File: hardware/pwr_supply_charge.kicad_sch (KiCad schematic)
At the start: 26 parts, among them J1 USB_C_Receptacle_USB2.0_14P, J2 Battery Input, J3 Power Switch, Q1 AO4435, Q2 AO4406A, Q3 AO4406A, Q4 AO4468, U1 CN3302, U2 HY2120

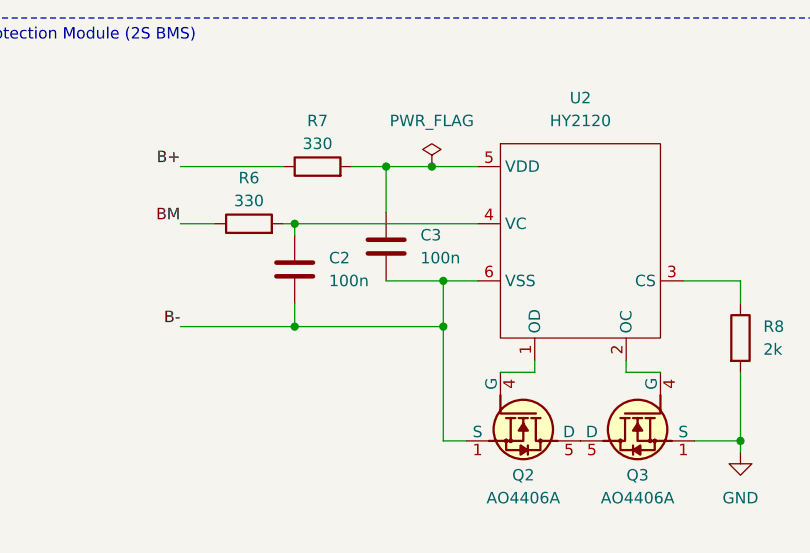
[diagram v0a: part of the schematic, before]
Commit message: Adding power LED status
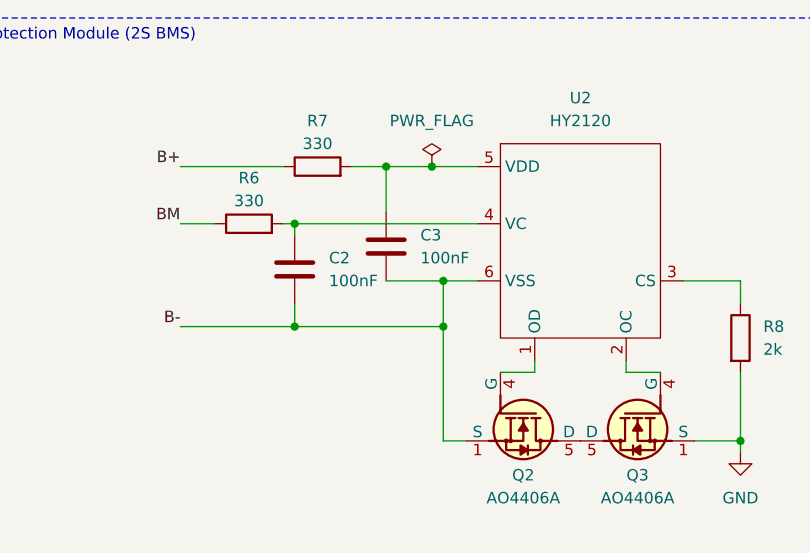
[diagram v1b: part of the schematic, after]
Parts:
- C2, C3: value 100n -> 100nF
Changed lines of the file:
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@@
 			)
 		)
-		(property "Value" "100n"
+		(property "Value" "100nF"
 			(at 180.34 41.9099 0)
 			(effects
@@
 			)
 		)
-		(property "Value" "100n"
+		(property "Value" "100nF"
 			(at 170.18 44.4499 0)
 			(effects

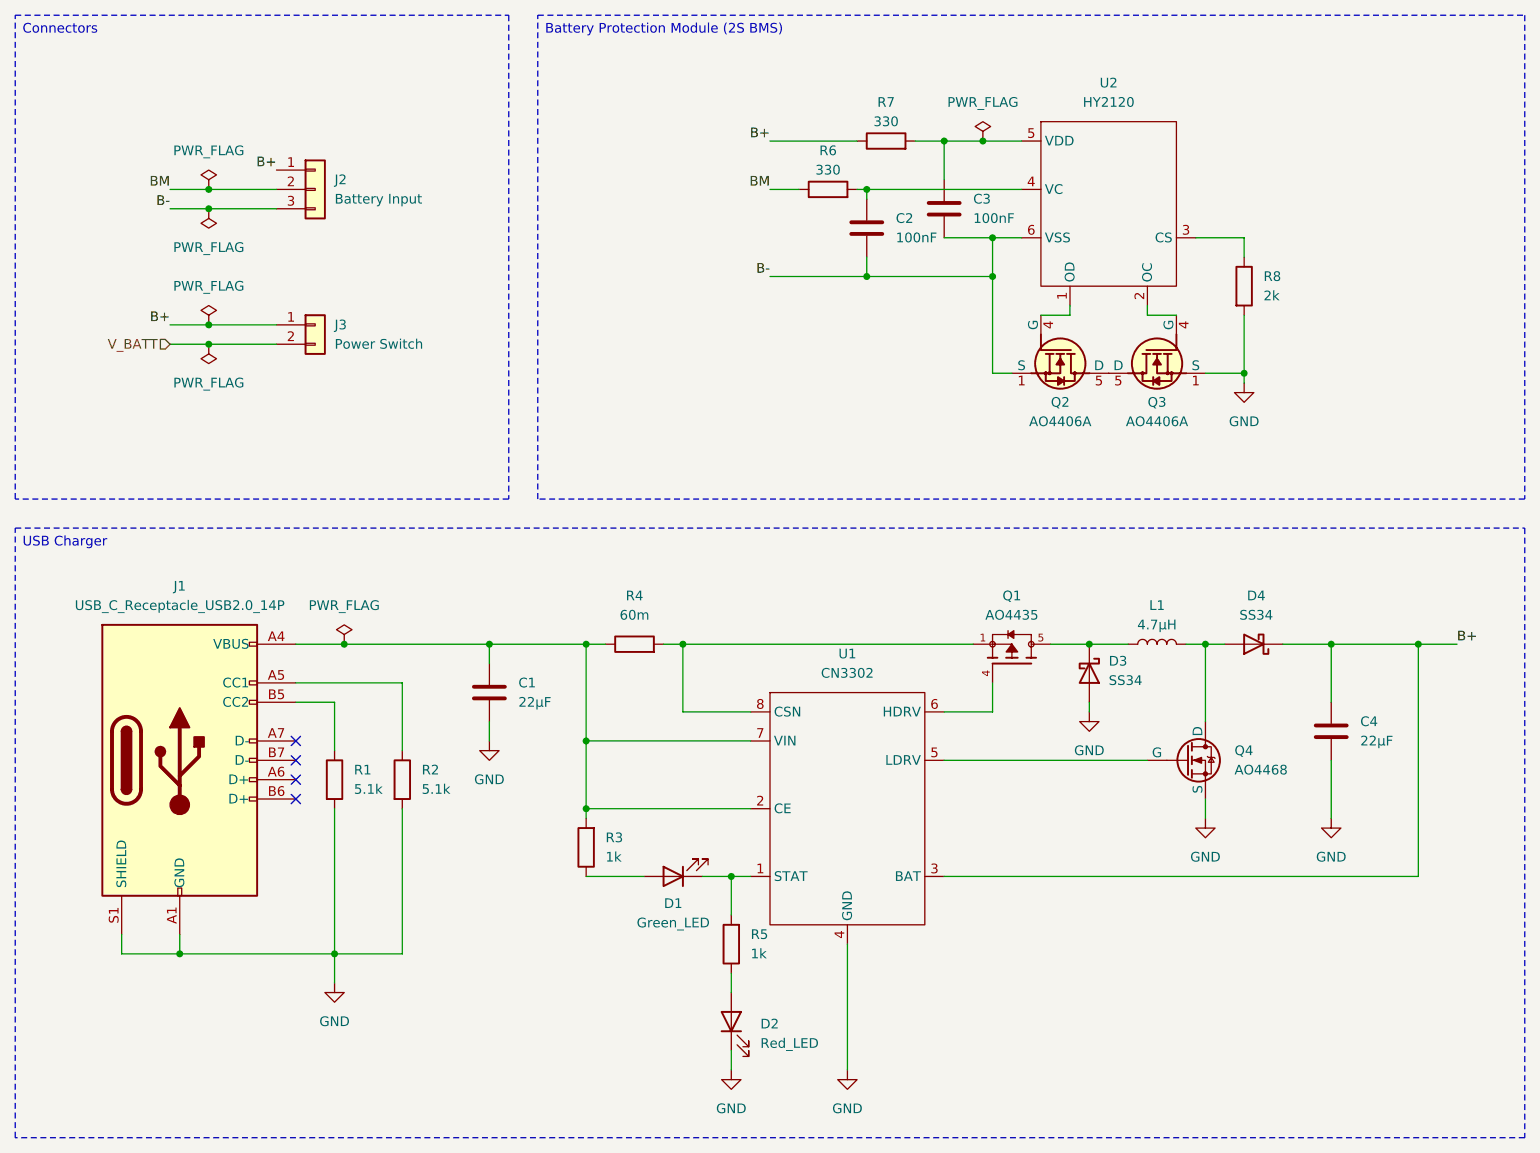
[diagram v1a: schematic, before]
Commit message: Adding footprint & symbol folders
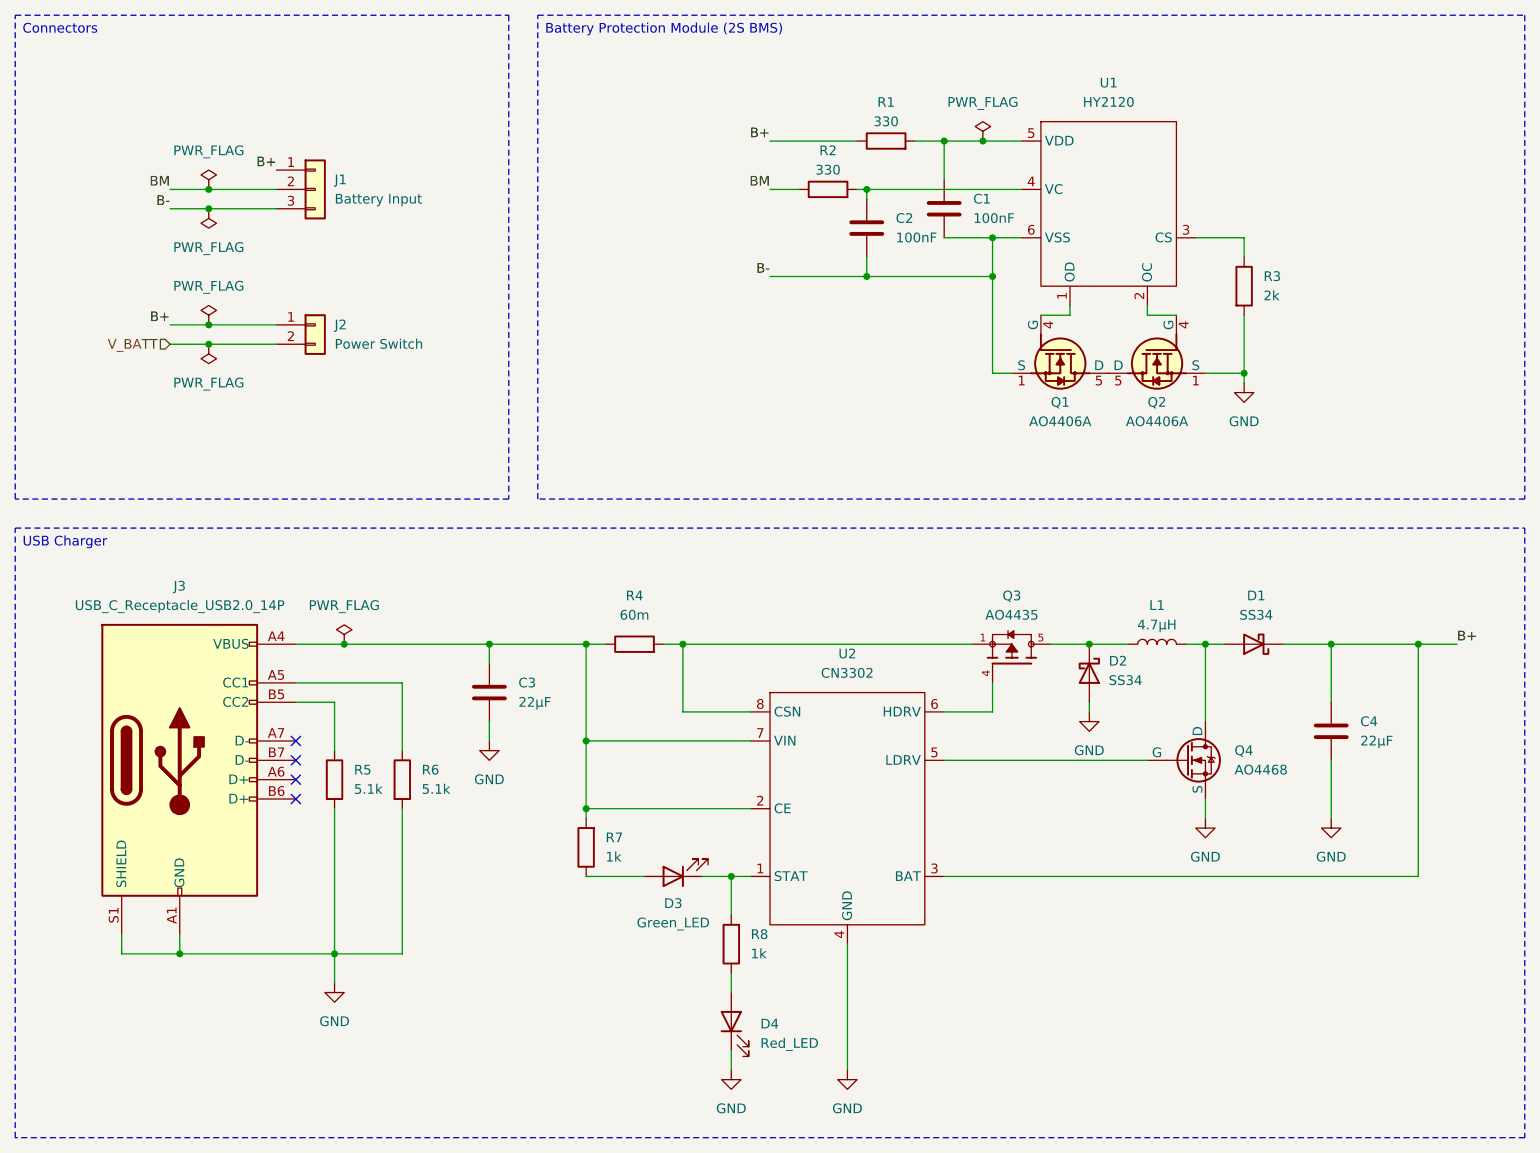
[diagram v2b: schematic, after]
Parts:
- removed Q1: AO4435, AO4435:SOIC127P600X175-8N, symbol AO4435:AO4435
- removed Q2, Q3: AO4406A, AO4406A:SOIC-8_3.9x4.9x1.75mm_P1.27mm, symbol AO4406A:AO4406A
- removed U1: CN3302, symbol _CN3302:CN3302
- removed U2: HY2120, symbol _HY2120:HY2120
- added Q1, Q2: AO4406A, Chromapi_FP:ao4406a_SOIC-8_3.9x4.9x1.75mm_P1.27mm, symbol ao4406a:AO4406A
- added Q3: AO4435, Chromapi_FP:ao4435_SOIC127P600X175-8N, symbol ao4435:AO4435
- added U1: HY2120, symbol hy2120:HY2120
- added U2: CN3302, symbol cn3302:CN3302
- renumbered C3 to C1, C1 to C3, D4 to D1, D3 to D2, D1 to D3, D2 to D4, J2 to J1, J3 to J2, J1 to J3, R7 to R1, R6 to R2, R8 to R3, R1 to R5, R2 to R6, R3 to R7, R5 to R8
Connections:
- net B+: now also U2.3 (BAT)
- net B-: now also Q1.1 (S), Q1.2 (S), Q1.3 (S), U1.6 (VSS)
- net GND: now also Q2.1 (S), Q2.2 (S), Q2.3 (S), U2.4 (GND)
- net at C1.1, R1.2: now also U1.5 (VDD)
- net at D3.1 (K), R8.2: now also U2.1 (STAT)
- net at R4.2: now also Q3.1, Q3.2, Q3.3, U2.8 (CSN)
- net at D2.1 (K), L1.1: now also Q3.5, Q3.6, Q3.7, Q3.8
- net at C3.1, J3.A4 (VBUS), J3.A9 (VBUS)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: now also U2.2 (CE), U2.7 (VIN)
- net at C2.1, R2.2: now also U1.4 (VC)
- net at R3.1: now also U1.3 (CS)
- net at Q4.2 (G): now also U2.5 (LDRV)
- new net: Q1.4 (G), U1.1 (OD)
- new net: Q2.4 (G), U1.2 (OC)
- new net: Q1.5 (D), Q1.6 (D), Q1.7 (D), Q1.8 (D), Q2.5 (D), Q2.6 (D), Q2.7 (D), Q2.8 (D)
- new net: Q3.4, U2.6 (HDRV)

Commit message: Adding cooling fan
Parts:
- D3, D4: footprint (none) -> LED_SMD:LED_0603_1608Metric
- J3: footprint (none) -> Connector_USB:USB_C_Receptacle_HRO_TYPE-C-31-M-12
- Q4: footprint (none) -> Chromapi_FP:ao4435_SOIC127P600X175-8N
- R5, R6, R7, R8: footprint (none) -> Resistor_SMD:R_0603_1608Metric
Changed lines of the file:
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@@
 			)
 		)
-		(property "Footprint" ""
+		(property "Footprint" "LED_SMD:LED_0603_1608Metric"
 			(at 140.97 128.27 0)
 			(effects
@@
 			)
 		)
-		(property "Footprint" ""
+		(property "Footprint" "Resistor_SMD:R_0603_1608Metric"
 			(at 150.368 137.16 90)
 			(effects
@@
 			)
 		)
-		(property "Footprint" ""
+		(property "Footprint" "Resistor_SMD:R_0603_1608Metric"
 			(at 131.318 124.46 90)
 			(effects
@@
 			)
 		)
-		(property "Footprint" ""
+		(property "Footprint" "Resistor_SMD:R_0603_1608Metric"
 			(at 94.742 115.57 90)
 			(effects
@@
 			)
 		)
-		(property "Footprint" ""
+		(property "Footprint" "Resistor_SMD:R_0603_1608Metric"
 			(at 103.632 115.57 90)
 			(effects
@@
 			)
 		)
-		(property "Footprint" ""
+		(property "Footprint" "Chromapi_FP:ao4435_SOIC127P600X175-8N"
 			(at 213.36 110.49 0)
 			(effects
@@
 			)
 		)
-		(property "Footprint" ""
+		(property "Footprint" "Connector_USB:USB_C_Receptacle_HRO_TYPE-C-31-M-12"
 			(at 80.01 113.03 0)
 			(effects
@@
 			)
 		)
-		(property "Footprint" ""
+		(property "Footprint" "LED_SMD:LED_0603_1608Metric"
 			(at 148.59 147.32 0)
 			(effects

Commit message: Adding footprints
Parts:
- U1: footprint (none) -> Package_TO_SOT_SMD:SOT-23-6
- U2: footprint (none) -> Package_SO:SOP-8_3.76x4.96mm_P1.27mm
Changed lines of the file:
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@@
 			)
 		)
-		(property "Footprint" ""
+		(property "Footprint" "Package_TO_SOT_SMD:SOT-23-6"
 			(at 198.12 39.37 0)
 			(effects
@@
 	)
 	(symbol
+		(lib_id "cn3302:CN3302")
+		(at 161.29 139.7 0)
+		(unit 1)
+		(exclude_from_sim no)
+		(in_bom yes)
+		(on_board yes)
+		(dnp no)
+		(fields_autoplaced yes)
+		(property "Reference" "U2"
+			(at 163.83 99.06 0)
+			(effects
+				(font
+					(size 1.27 1.27)
+				)
+			)
+		)
+		(property "Value" "CN3302"
+			(at 163.83 101.6 0)
+			(effects
+				(font
+					(size 1.27 1.27)
+				)
+			)
+		)
+		(property "Footprint" "Package_SO:SOP-8_3.76x4.96mm_P1.27mm"
+			(at 161.29 139.7 0)
+			(effects
+				(font
+					(size 1.27 1.27)
+				)
+				(hide yes)
+			)
+		)
+		(property "Datasheet" "https://github.com/Mowibox/chromapi_motherboard/blob/main/docs/datasheets/CN3302.pdf"
+			(at 161.29 139.7 0)
+			(effects
+				(font
+					(size 1.27 1.27)
+				)
+				(hide yes)
+			)
+		)
+		(property "Description" "PFM Step-up 2-cell Lithium Battery Charger IC"
+			(at 161.29 139.7 0)
+			(effects
+				(font
+					(size 1.27 1.27)
+				)
+				(hide yes)
+			)
+		)
+		(pin "3"
+		)
+		(pin "5"
+		)
+		(pin "1"
+		)
+		(pin "8"
+		)
+		(pin "4"
+		)
+		(pin "2"
+		)
+		(pin "6"
+		)
+		(pin "7"
+		)
+		(instances
+			(project ""
+				(path "/d1a31f26-03e0-43e1-89c1-031fe31befc5/2dc5047f-e6b9-4c1e-8ac3-300835122eb4"
+					(reference "U2")
+					(unit 1)
+				)
+			)
+		)
+	)
+	(symbol
+		(lib_id "power:GND")
+		(at 96.52 142.24 0)
+		(unit 1)
+		(exclude_from_sim no)
+		(in_bom yes)
+		(on_board yes)
+		(dnp no)
+		(fields_autoplaced yes)
+		(property "Reference" "#PWR07"
+			(at 96.52 148.59 0)
+			(effects
+				(font
+					(size 1.27 1.27)
+				)
+				(hide yes)
+			)
+		)
+		(property "Value" "GND"
+			(at 96.52 147.32 0)
+			(effects
+				(font
+					(size 1.27 1.27)
+				)
+			)
+		)
+		(property "Footprint" ""
+			(at 96.52 142.24 0)
+			(effects
+				(font
+					(size 1.27 1.27)
+				)
+				(hide yes)
+			)
+		)
+		(property "Datasheet" ""
+			(at 96.52 142.24 0)
+			(effects
+				(font
+					(size 1.27 1.27)
+				)
+				(hide yes)
+			)
+		)
+		(property "Description" "Power symbol creates a global label with name \"GND\" , ground"
+			(at 96.52 142.24 0)
+			(effects
+				(font
+					(size 1.27 1.27)
+				)
+				(hide yes)
+			)
+		)
+		(pin "1"
+		)
+		(instances
+			(project ""
+				(path "/d1a31f26-03e0-43e1-89c1-031fe31befc5/2dc5047f-e6b9-4c1e-8ac3-300835122eb4"
+					(reference "#PWR07")
+					(unit 1)
+				)
+			)
+		)
+	)
+	(symbol
 		(lib_id "ao4406a:AO4406A")
 		(at 207.01 55.88 90)
@@
 					(unit 1)
 				)
-			)
-		)
-	)
-	(symbol
-		(lib_id "cn3302:CN3302")
-		(at 161.29 139.7 0)
-		(unit 1)
-		(exclude_from_sim no)
-		(in_bom yes)
-		(on_board yes)
-		(dnp no)
-		(fields_autoplaced yes)
-		(property "Reference" "U2"
-			(at 163.83 99.06 0)
-			(effects
-				(font
-					(size 1.27 1.27)
-				)
-			)
-		)
-		(property "Value" "CN3302"
-			(at 163.83 101.6 0)
-			(effects
-				(font
-					(size 1.27 1.27)
-				)
-			)
-		)
-		(property "Footprint" ""
-			(at 161.29 139.7 0)
-			(effects
-				(font
-					(size 1.27 1.27)
-				)
-				(hide yes)
-			)
-		)
-		(property "Datasheet" "https://github.com/Mowibox/chromapi_motherboard/blob/main/docs/datasheets/CN3302.pdf"
-			(at 161.29 139.7 0)
-			(effects
-				(font
-					(size 1.27 1.27)
-				)
-				(hide yes)
-			)
-		)
-		(property "Description" "PFM Step-up 2-cell Lithium Battery Charger IC"
-			(at 161.29 139.7 0)
-			(effects
-				(font
-					(size 1.27 1.27)
-				)
-				(hide yes)
-			)
-		)
-		(pin "3"
-		)
-		(pin "5"
-		)
-		(pin "1"
-		)
-		(pin "8"
-		)
-		(pin "4"
-		)
-		(pin "2"
-		)
-		(pin "6"
-		)
-		(pin "7"
-		)
-		(instances
-			(project ""
-				(path "/d1a31f26-03e0-43e1-89c1-031fe31befc5/2dc5047f-e6b9-4c1e-8ac3-300835122eb4"
-					(reference "U2")
-					(unit 1)
-				)
-			)
-		)
-	)
-	(symbol
-		(lib_id "power:GND")
-		(at 96.52 142.24 0)
-		(unit 1)
-		(exclude_from_sim no)
-		(in_bom yes)
-		(on_board yes)
-		(dnp no)
-		(fields_autoplaced yes)
-		(property "Reference" "#PWR07"
-			(at 96.52 148.59 0)
-			(effects
-				(font
-					(size 1.27 1.27)
-				)
-				(hide yes)
-			)
-		)
-		(property "Value" "GND"
-			(at 96.52 147.32 0)
-			(effects
-				(font
-					(size 1.27 1.27)
-				)
-			)
-		)
-		(property "Footprint" ""
-			(at 96.52 142.24 0)
-			(effects
-				(font
-					(size 1.27 1.27)
-				)
-				(hide yes)
-			)
-		)
-		(property "Datasheet" ""
-			(at 96.52 142.24 0)
-			(effects
-				(font
-					(size 1.27 1.27)
-				)
-				(hide yes)
-			)
-		)
-		(property "Description" "Power symbol creates a global label with name \"GND\" , ground"
-			(at 96.52 142.24 0)
-			(effects
-				(font
-					(size 1.27 1.27)
-				)
-				(hide yes)
-			)
-		)
-		(pin "1"
-		)
-		(instances
-			(project ""
-				(path "/d1a31f26-03e0-43e1-89c1-031fe31befc5/2dc5047f-e6b9-4c1e-8ac3-300835122eb4"
-					(reference "#PWR07")
-					(unit 1)
-				)

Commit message: Updating footprints
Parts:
- C1, C2: footprint (none) -> Capacitor_SMD:C_0201_0603Metric
- C3, C4: footprint (none) -> Capacitor_SMD:C_0805_2012Metric
- J1, L1: footprint (none) -> Connector_AMASS:AMASS_XT30PW-M_1x02_P2.50mm_Horizontal
- J2: footprint (none) -> Connector_JST:JST_XH_B2B-XH-A_1x02_P2.50mm_Vertical
- R1, R2, R3, R4: footprint (none) -> Resistor_SMD:R_0603_1608Metric
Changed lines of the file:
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@@
 			)
 		)
-		(property "Footprint" ""
+		(property "Footprint" "Resistor_SMD:R_0603_1608Metric"
 			(at 168.91 33.528 90)
 			(effects
@@
 			)
 		)
-		(property "Footprint" ""
+		(property "Footprint" "Connector_JST:JST_XH_B2B-XH-A_1x02_P2.50mm_Vertical"
 			(at 93.98 55.88 0)
 			(effects
@@
 			)
 		)
-		(property "Footprint" ""
+		(property "Footprint" "Capacitor_SMD:C_0805_2012Metric"
 			(at 228.2952 113.03 0)
 			(effects
@@
 			)
 		)
-		(property "Footprint" ""
+		(property "Footprint" "Resistor_SMD:R_0603_1608Metric"
 			(at 135.89 99.568 90)
 			(effects
@@
 			)
 		)
-		(property "Footprint" ""
+		(property "Footprint" "Connector_AMASS:AMASS_XT30PW-M_1x02_P2.50mm_Horizontal"
 			(at 93.98 38.1 0)
 			(effects
@@
 			)
 		)
-		(property "Footprint" ""
+		(property "Footprint" "Resistor_SMD:R_0603_1608Metric"
 			(at 161.29 39.878 90)
 			(effects
@@
 			)
 		)
-		(property "Footprint" ""
+		(property "Footprint" "Resistor_SMD:R_0603_1608Metric"
 			(at 214.122 50.8 90)
 			(effects
@@
 			)
 		)
-		(property "Footprint" ""
+		(property "Footprint" "Connector_AMASS:AMASS_XT30PW-M_1x02_P2.50mm_Horizontal"
 			(at 204.47 97.79 0)
 			(effects
@@
 			)
 		)
-		(property "Footprint" ""
+		(property "Footprint" "Capacitor_SMD:C_0805_2012Metric"
 			(at 117.8052 107.95 0)
 			(effects
@@
 			)
 		)
-		(property "Footprint" ""
+		(property "Footprint" "Capacitor_SMD:C_0201_0603Metric"
 			(at 177.4952 44.45 0)
 			(effects
@@
 			)
 		)
-		(property "Footprint" ""
+		(property "Footprint" "Capacitor_SMD:C_0201_0603Metric"
 			(at 167.3352 46.99 0)
 			(effects
